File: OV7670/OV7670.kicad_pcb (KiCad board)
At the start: 2 copper layers, 24 x 41 mm, 9 parts, among them J1 OV7670, J2 PMOD1, J3 PMOD2, J4 PMOD1_EXT, J6 EXT1

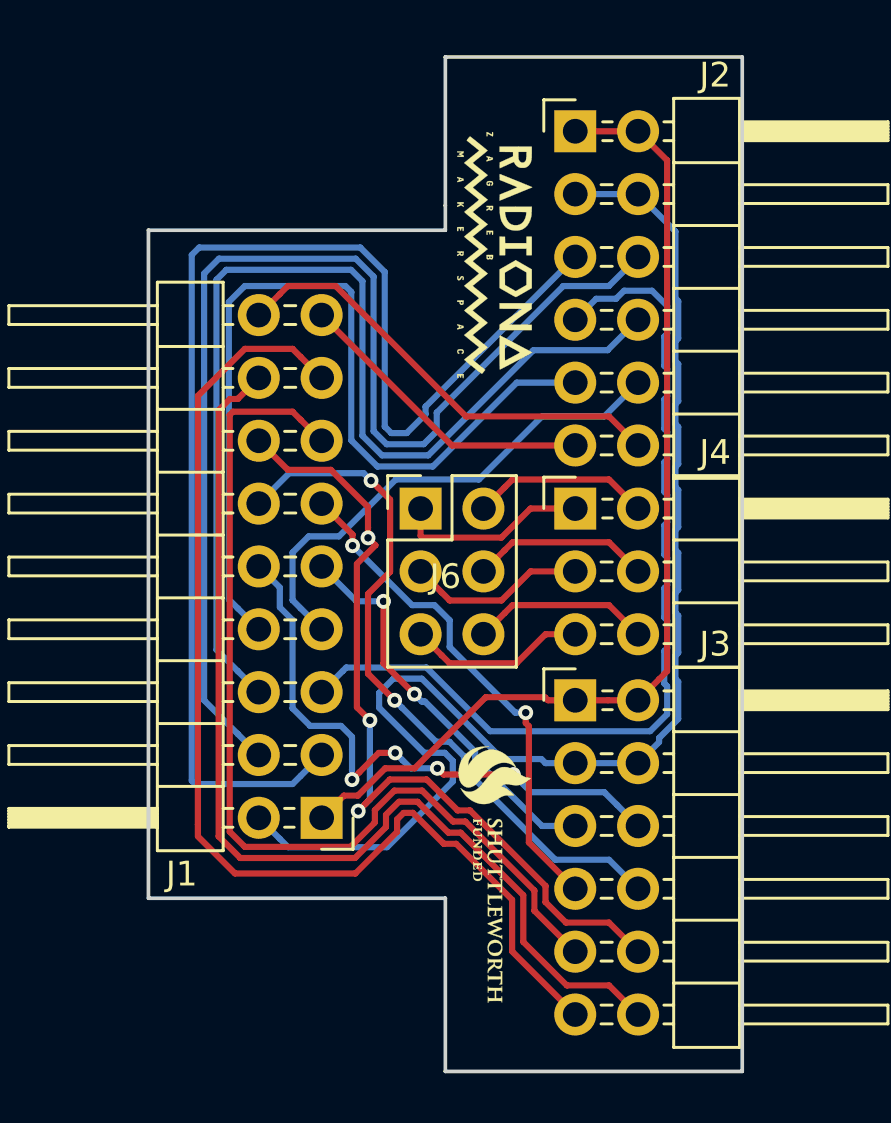
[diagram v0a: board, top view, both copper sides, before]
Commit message: Adding GND and VCC to EXT connector
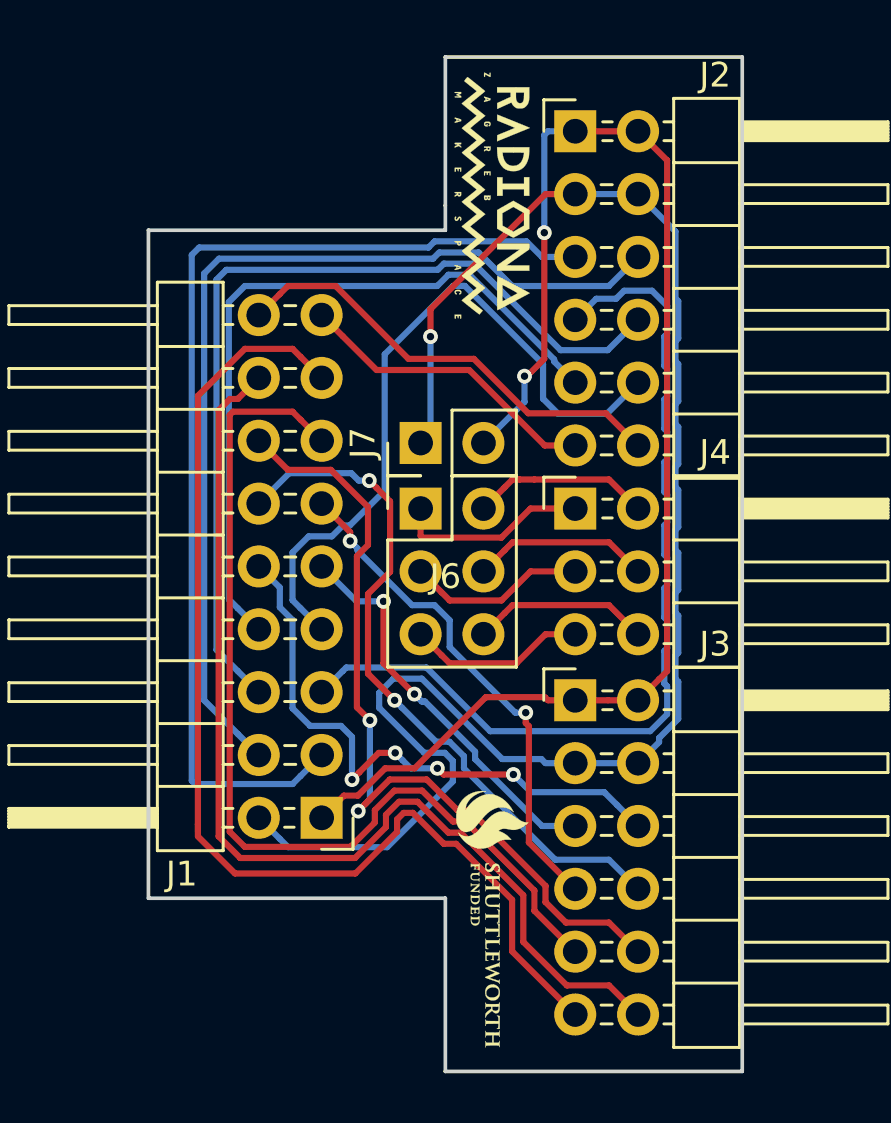
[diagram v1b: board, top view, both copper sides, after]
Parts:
- added J7: EXTVCC, Connector_PinHeader_2.54mm:PinHeader_1x02_P2.54mm_Vertical, F.Cu at (151.0, 71.6)
- ? (x4): renamed from G***; value LOGO -> (none)
- moved ? 2.40 mm to (153.9, 61.6) (x2)
- moved ? 1.90 mm to (153.9, 90.9)
- moved ? 1.80 mm to (153.9, 90.8)
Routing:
- net 3V3: track 41.4 -> 56.2 mm, vias 0 -> 2
- net GND: track 54.3 -> 67.7 mm, vias 0 -> 1
- net SIOC: track 52.6 -> 43.0 mm
- net SIOD: track 48.5 -> 39.3 mm
- net PCLK: track 20.4 -> 28.7 mm
- net HREF: track 43.6 -> 36.6 mm
- net XCLK: track 35.9 -> 30.0 mm
- net D2: track 33.8 -> 33.5 mm, vias 3 -> 2

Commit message: Adding text
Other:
- board text added: "TOP"
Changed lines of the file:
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@@
-(kicad_pcb (version 20171130) (host pcbnew 5.0.1+dfsg1-3~bpo9+1)
+(kicad_pcb (version 20171130) (host pcbnew 5.0.2+dfsg1-1)
   (general
     (thickness 1.6)
-    (drawings 51)
+    (drawings 53)
     (tracks 361)
     (zones 0)
@@
       (net 1 3V3))
   )
+  (gr_text TOP (at 152.6 82.2) (layer F.SilkS)
+    (effects (font (size 1.5 1.5) (thickness 0.3)))
+  )
+  (gr_text TOP (at 152.4 69) (layer F.SilkS)
+    (effects (font (size 1.5 1.5) (thickness 0.3)))
+  )
   (gr_line (start 140 63) (end 140 90) (layer Edge.Cuts) (width 0.15))

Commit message: Adding ISH park logo
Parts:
- added G***: LOGO, parts:OSH_2_5x2_5, B.Cu at (150.0, 87.8)
- added G***: LOGO, parts:OSH_2_5x2_5, B.Cu at (150.2, 65.4)
- moved ? 0.51 mm to (154.4, 91.0)

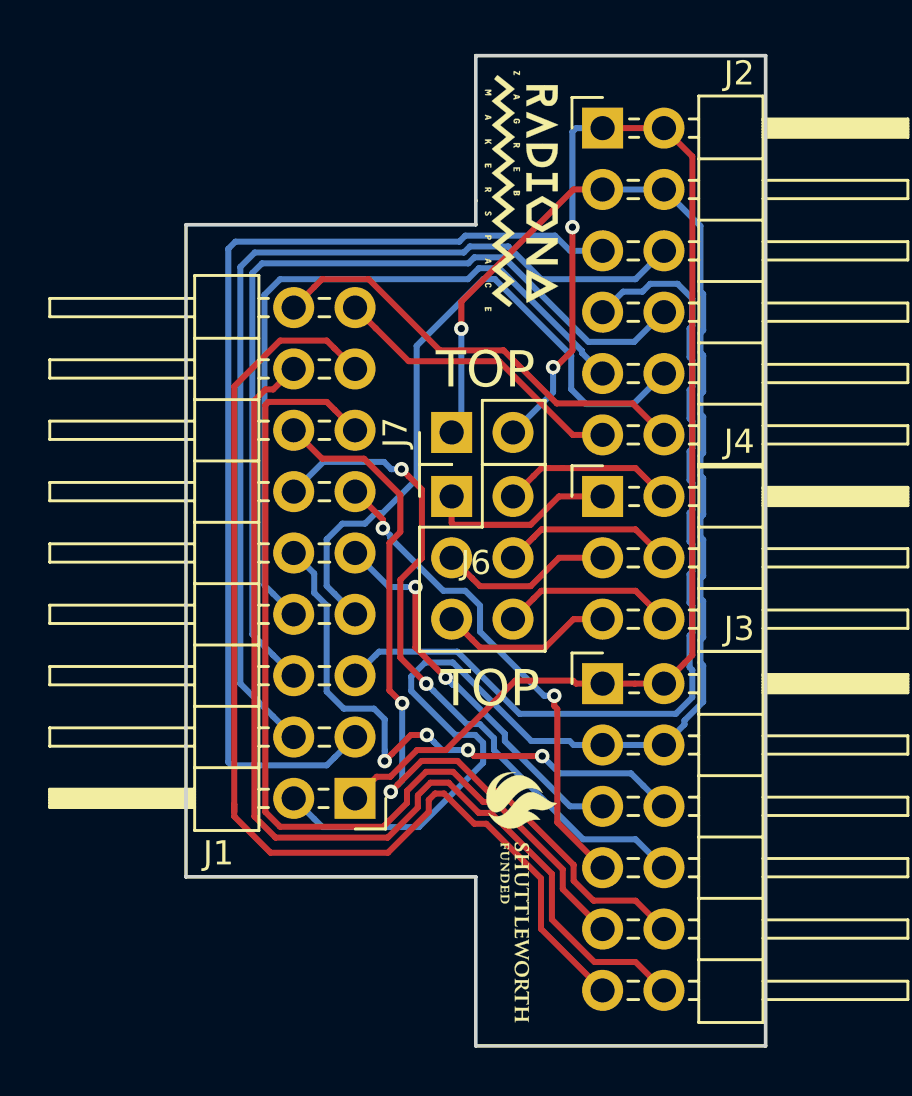
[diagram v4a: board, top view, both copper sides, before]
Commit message: Adding new OV7670 with gerber zip
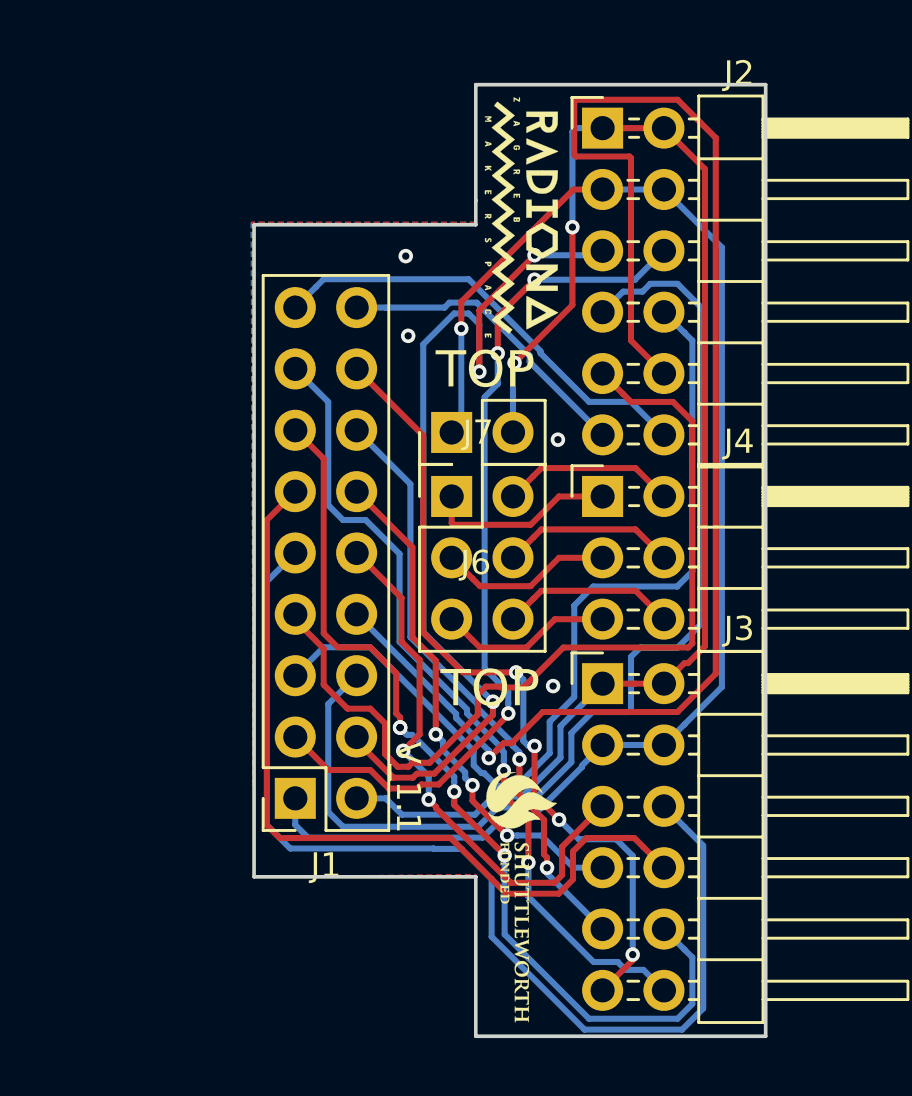
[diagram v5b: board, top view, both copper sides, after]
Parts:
- J1: footprint Connector_PinHeader_2.54mm:PinHeader_2x09_P2.54mm_Horizontal -> Connector_PinSocket_2.54mm:PinSocket_2x09_P2.54mm_Vertical
- moved J1 2.47 mm to (144.5, 86.8)
- moved ? 1.20 mm to (153.9, 62.8)
- moved ? 1.10 mm to (153.9, 62.7)
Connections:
- J1 pad 1: 3V3 -> GND
- J1 pad 10: D6 -> D7
- J1 pad 11: D5 -> D4
- J1 pad 12: D4 -> D5
- J1 pad 13: D3 -> D2
- J1 pad 14: D2 -> D3
- J1 pad 15: D1 -> D0
- J1 pad 16: D0 -> D1
- J1 pad 17: RESET -> PWDN
- J1 pad 18: PWDN -> RESET
- J1 pad 2: GND -> 3V3
- J1 pad 3: SIOC -> SIOD
- J1 pad 4: SIOD -> SIOC
- J1 pad 5: VSYNC -> HREF
- J1 pad 6: HREF -> VSYNC
- J1 pad 7: PCLK -> XCLK
- J1 pad 8: XCLK -> PCLK
- J1 pad 9: D7 -> D6
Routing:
- net PCLK: track 28.7 -> 61.9 mm, vias 0 -> 1
- net D6: track 24.1 -> 44.1 mm, vias 4 -> 0
- net D3: track 39.7 -> 24.9 mm, vias 0 -> 2
- net D1: track 46.2 -> 33.3 mm, vias 0 -> 4
- net D0: track 42.6 -> 33.6 mm, vias 0 -> 2
- net GND: track 67.7 -> 59.1 mm, vias 1 -> 5
- net VSYNC: track 37.3 -> 45.5 mm
- net XCLK: track 30.0 -> 37.2 mm
- net D7: track 16.2 -> 22.7 mm
- net D2: track 33.5 -> 39.2 mm, vias 2 -> 4
- net D4: track 28.4 -> 34.1 mm, vias 2 -> 0
- net SIOC: track 43.0 -> 37.7 mm, vias 0 -> 3
- net SIOD: track 39.3 -> 36.1 mm, vias 0 -> 3
- net 3V3: track 56.2 -> 57.8 mm
- net HREF: track 36.6 -> 37.5 mm
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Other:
- board size 24 x 41 mm -> 21.2 x 39.4 mm
- board text added: "V_1.1"

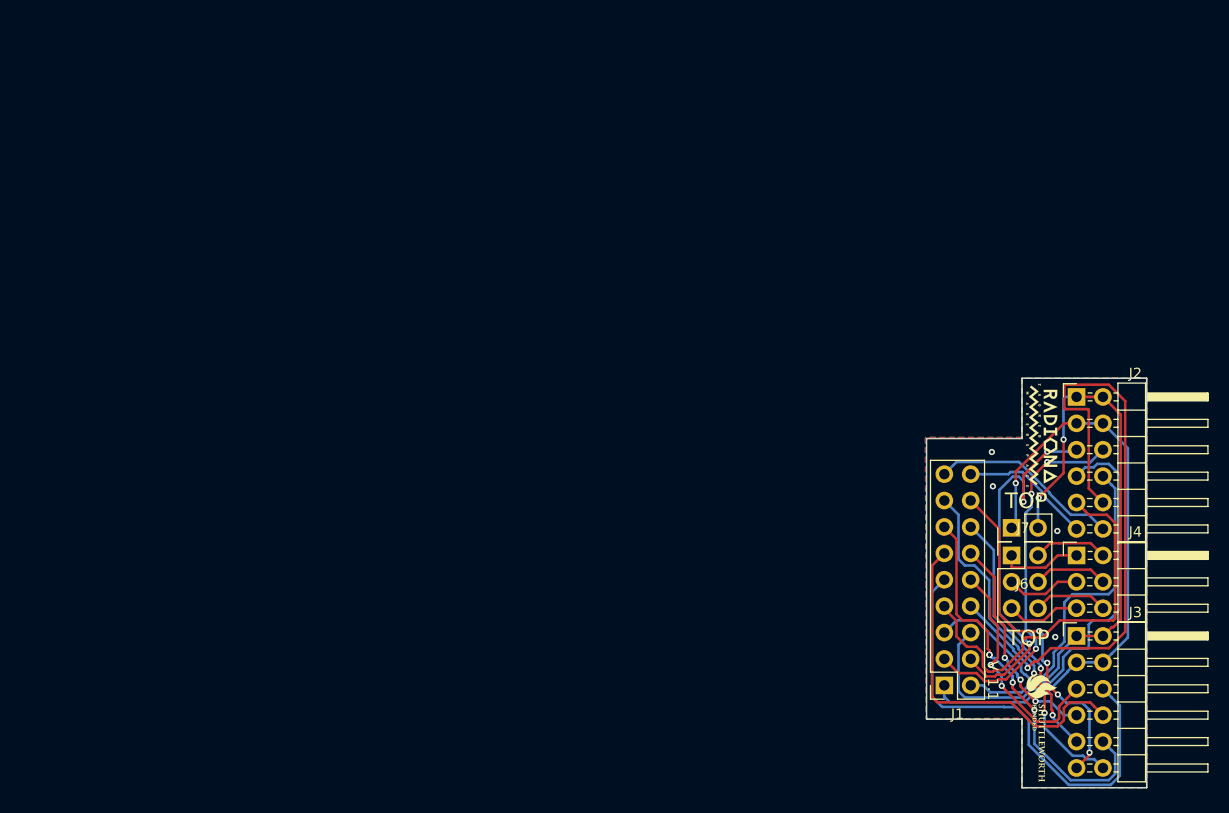
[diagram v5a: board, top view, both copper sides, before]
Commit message: OV7670 update
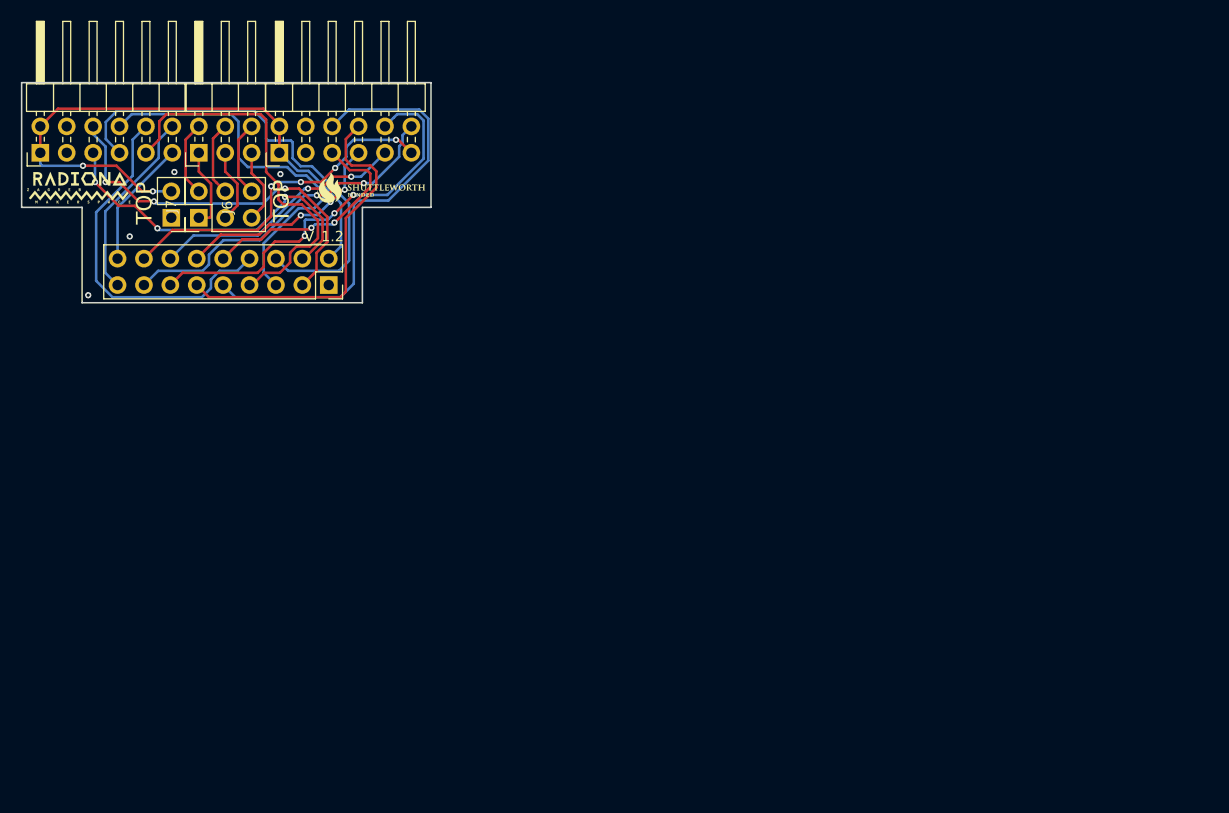
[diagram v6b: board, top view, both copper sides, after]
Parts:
- removed the G*** at (150.0, 87.8)
- removed the G*** at (150.2, 65.4)
- added G***: LOGO, intergalaktik:intergalaktik, B.Cu at (75.3, 43.8)
- moved J2 102.4 mm to (57.5, 35.5), turned to 90 degrees
- moved ? 95.7 mm to (61.2, 38.9), turned to 0 degrees
- moved ? 95.6 mm to (61.4, 38.9), turned to 180 degrees
- moved J4 92.9 mm to (72.8, 35.5), turned to 90 degrees
- moved J3 89.7 mm to (80.5, 35.5), turned to 90 degrees
- moved J7 86.2 mm to (70.2, 41.8), turned to 180 degrees
- moved J6 84.7 mm to (72.8, 41.8), turned to 90 degrees
- moved ? 83.5 mm to (89.5, 38.4), turned to 180 degrees
- moved ? 82.9 mm to (89.3, 38.9), turned to 0 degrees
- moved J1 70.6 mm to (85.3, 48.2), turned to -90 degrees
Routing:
- net GND: track 59.1 -> 0.00 mm, vias 5 -> 4
- net PCLK: track 61.9 -> 34.3 mm, vias 1 -> 0
- net SIOC: track 37.7 -> 33.9 mm
- net SIOD: track 36.1 -> 37.3 mm
- net VSYNC: track 45.5 -> 46.4 mm
- net D4: track 34.1 -> 35.0 mm
- net XCLK: track 37.2 -> 37.8 mm
- net D2: vias 4 -> 3
- added copper zone on In1.Cu, net GND
- added copper zone on In2.Cu, net GND
- removed copper zone on B.Cu, net GND
- removed copper zone on F.Cu, net GND
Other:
- board size 21.2 x 39.4 mm -> 39.4 x 21.2 mm
- copper layers 2 -> 4
- net class Default removed
- board text added: "V_1.2"
- board text removed: "V_1.1"
